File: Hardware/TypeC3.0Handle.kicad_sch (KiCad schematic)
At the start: 65 parts

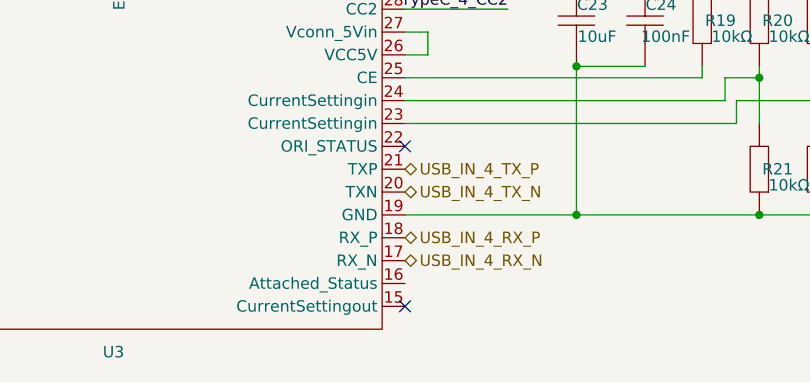
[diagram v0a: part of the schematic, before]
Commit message: 完成HUB部分原理图绘制
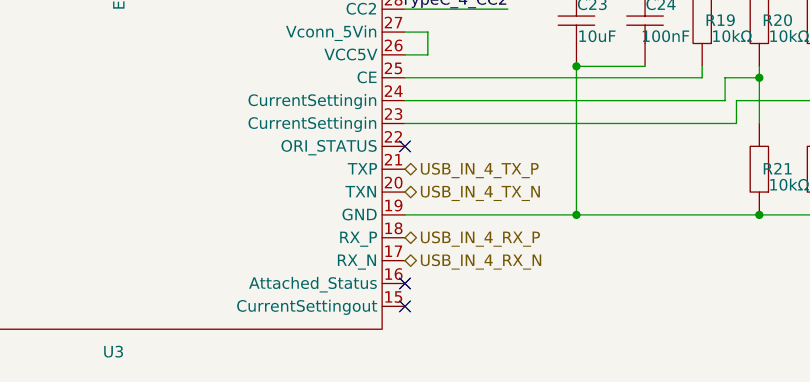
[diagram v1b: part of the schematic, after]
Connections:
- no-connect marks 31 -> 32
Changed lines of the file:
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@@
+	)
+	(no_connect
+		(at -16.51 252.73)
 	)
 	(no_connect

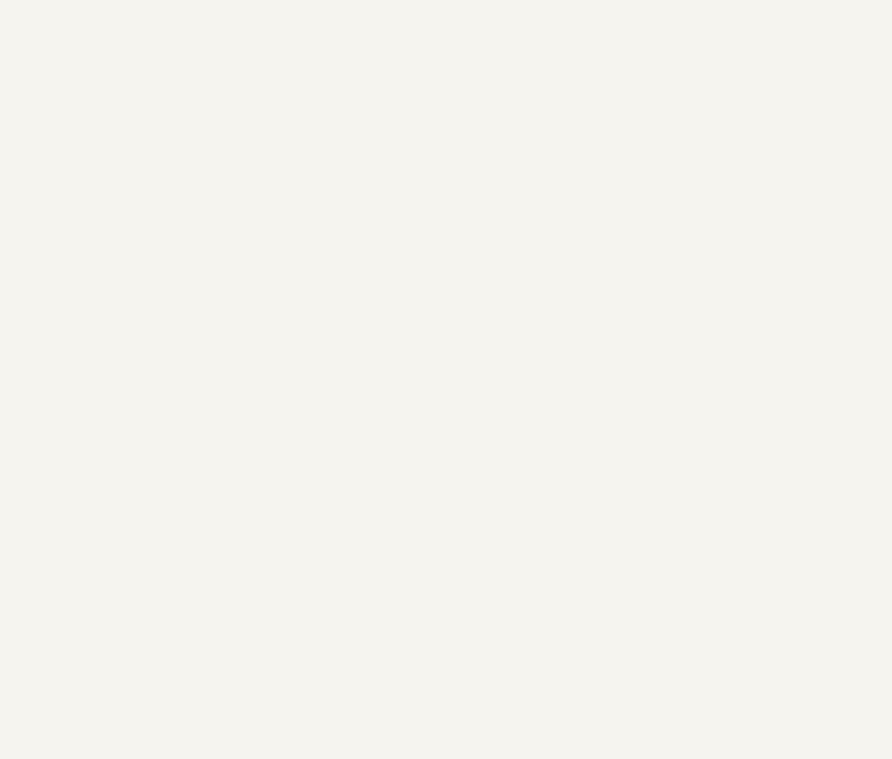
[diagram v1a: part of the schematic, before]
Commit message: 完成除MCU外的设计
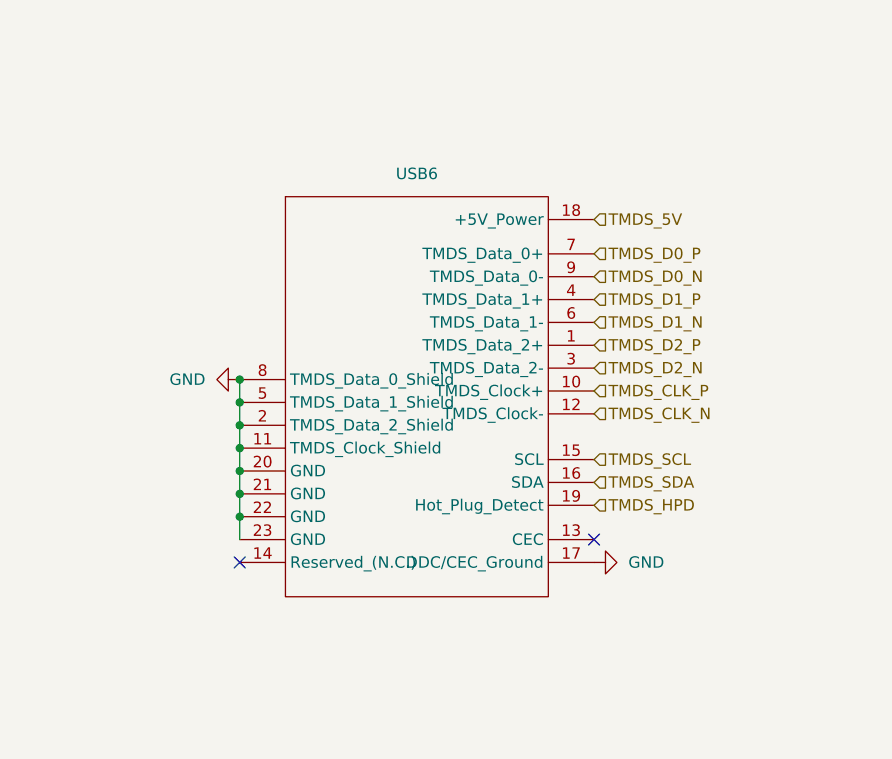
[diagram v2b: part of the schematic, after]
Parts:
- added USB6: ~, persional_library:HDMI-SMD_HDMI-001S, symbol persional_library:Connect_HDMI_001S
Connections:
- net GND: now also USB6.11 (TMDS_Clock_Shield), USB6.17 (DDC/CEC_Ground), USB6.2 (TMDS_Data_2_Shield), USB6.20 (GND), USB6.21 (GND), USB6.22 (GND), USB6.23 (GND), USB6.5 (TMDS_Data_1_Shield), USB6.8 (TMDS_Data_0_Shield)
- new net TMDS_5V: USB6.18 (+5V_Power)
- new net TMDS_CLK_N: USB6.12 (TMDS_Clock-)
- new net TMDS_CLK_P: USB6.10 (TMDS_Clock+)
- new net TMDS_D0_N: USB6.9 (TMDS_Data_0-)
- new net TMDS_D0_P: USB6.7 (TMDS_Data_0+)
- new net TMDS_D1_N: USB6.6 (TMDS_Data_1-)
- new net TMDS_D1_P: USB6.4 (TMDS_Data_1+)
- new net TMDS_D2_N: USB6.3 (TMDS_Data_2-)
- new net TMDS_D2_P: USB6.1 (TMDS_Data_2+)
- new net TMDS_HPD: USB6.19 (Hot_Plug_Detect)
- new net TMDS_SCL: USB6.15 (SCL)
- new net TMDS_SDA: USB6.16 (SDA)
- no-connect marks 32 -> 34

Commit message: 开始PCB布局
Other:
- note added: "HDMI输入"
- note added: "HUB的上游TypeC"
- note added: "TypeC转HDMI输入"
- note added: "TypeC转USB3.0"
- moved on the sheet: C1, C10, C11, C12, C13, C14, C15, C16, C17, C18, C19, C2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
